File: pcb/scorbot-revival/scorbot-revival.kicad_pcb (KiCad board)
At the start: 2 copper layers, 30.5 x 76.2 mm, 4 parts, among them J1 DB-50, J2 Raspberry_Pi_2_3, U1 L293D, U2 PIC18F2431-E_SP

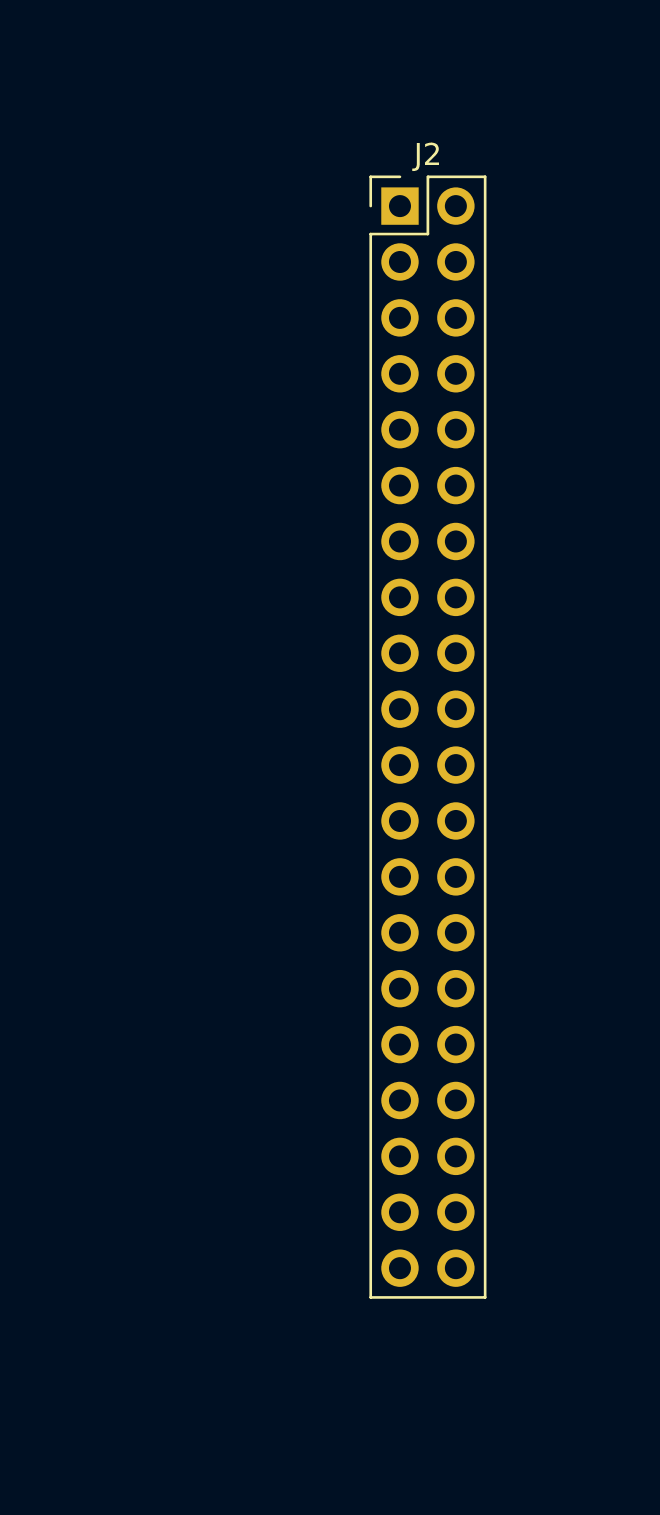
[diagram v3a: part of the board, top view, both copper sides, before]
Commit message: [pcb] update schematic connections
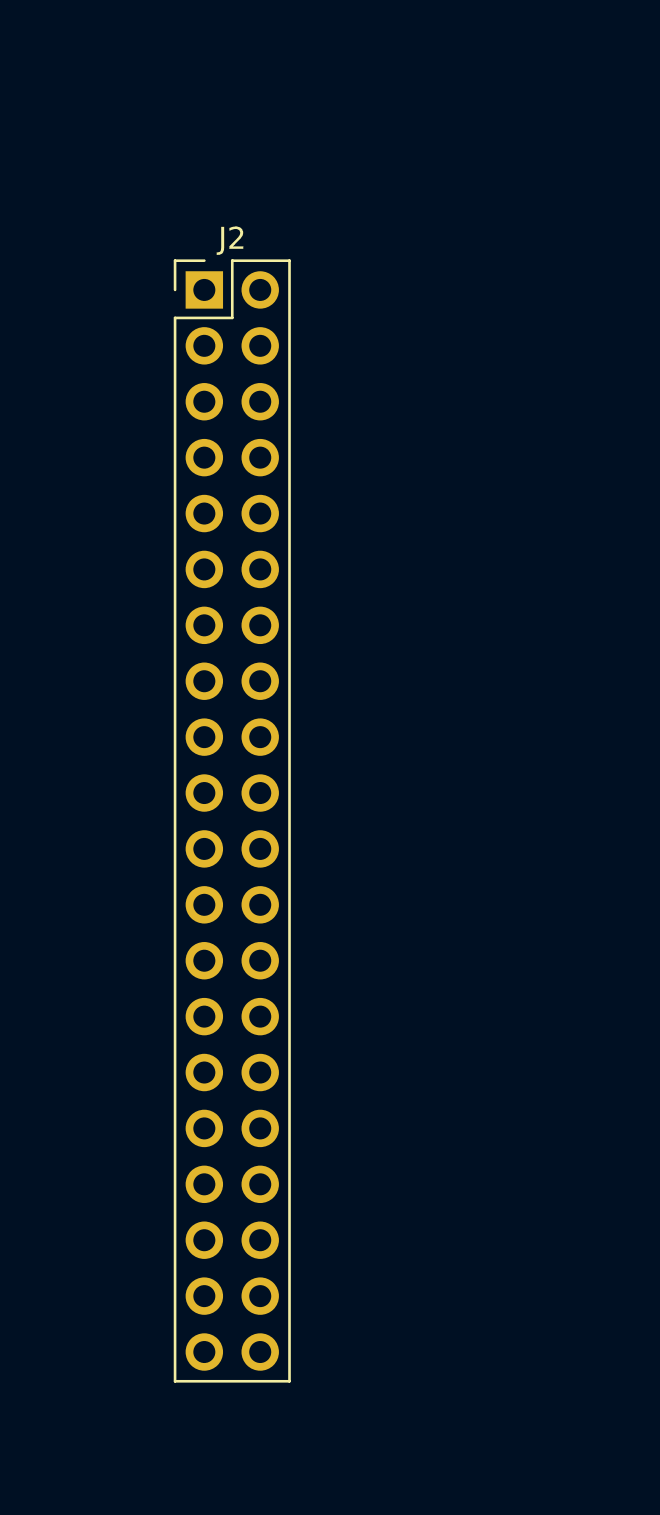
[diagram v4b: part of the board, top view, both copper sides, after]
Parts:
- moved J2 9.67 mm to (91.4, 30.5)
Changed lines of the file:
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@@
   )
   (module Connector_PinHeader_2.54mm:PinHeader_2x20_P2.54mm_Vertical (layer F.Cu)
-    (at 100.33 26.67)
+    (at 91.44 30.48)
     (descr "Through hole straight pin header, 2x20, 2.54mm pitch, double rows")
     (tags "Through hole pin header THT 2x20 2.54mm double row")

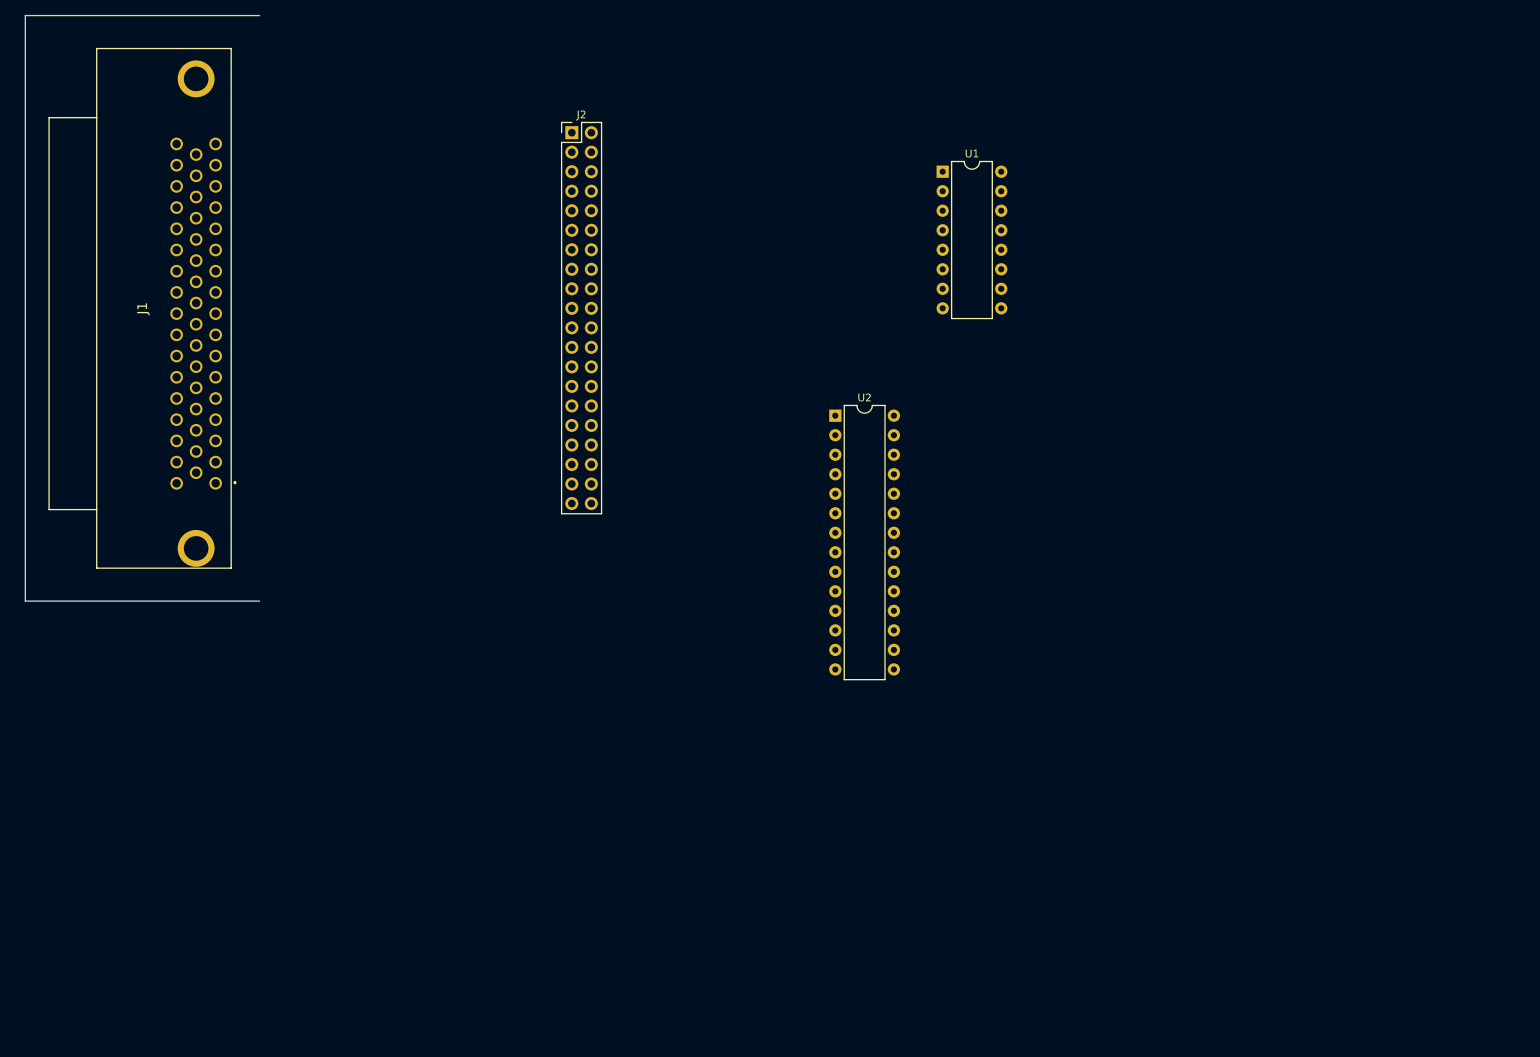
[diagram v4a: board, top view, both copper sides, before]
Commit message: [pcb] pcbnew updates
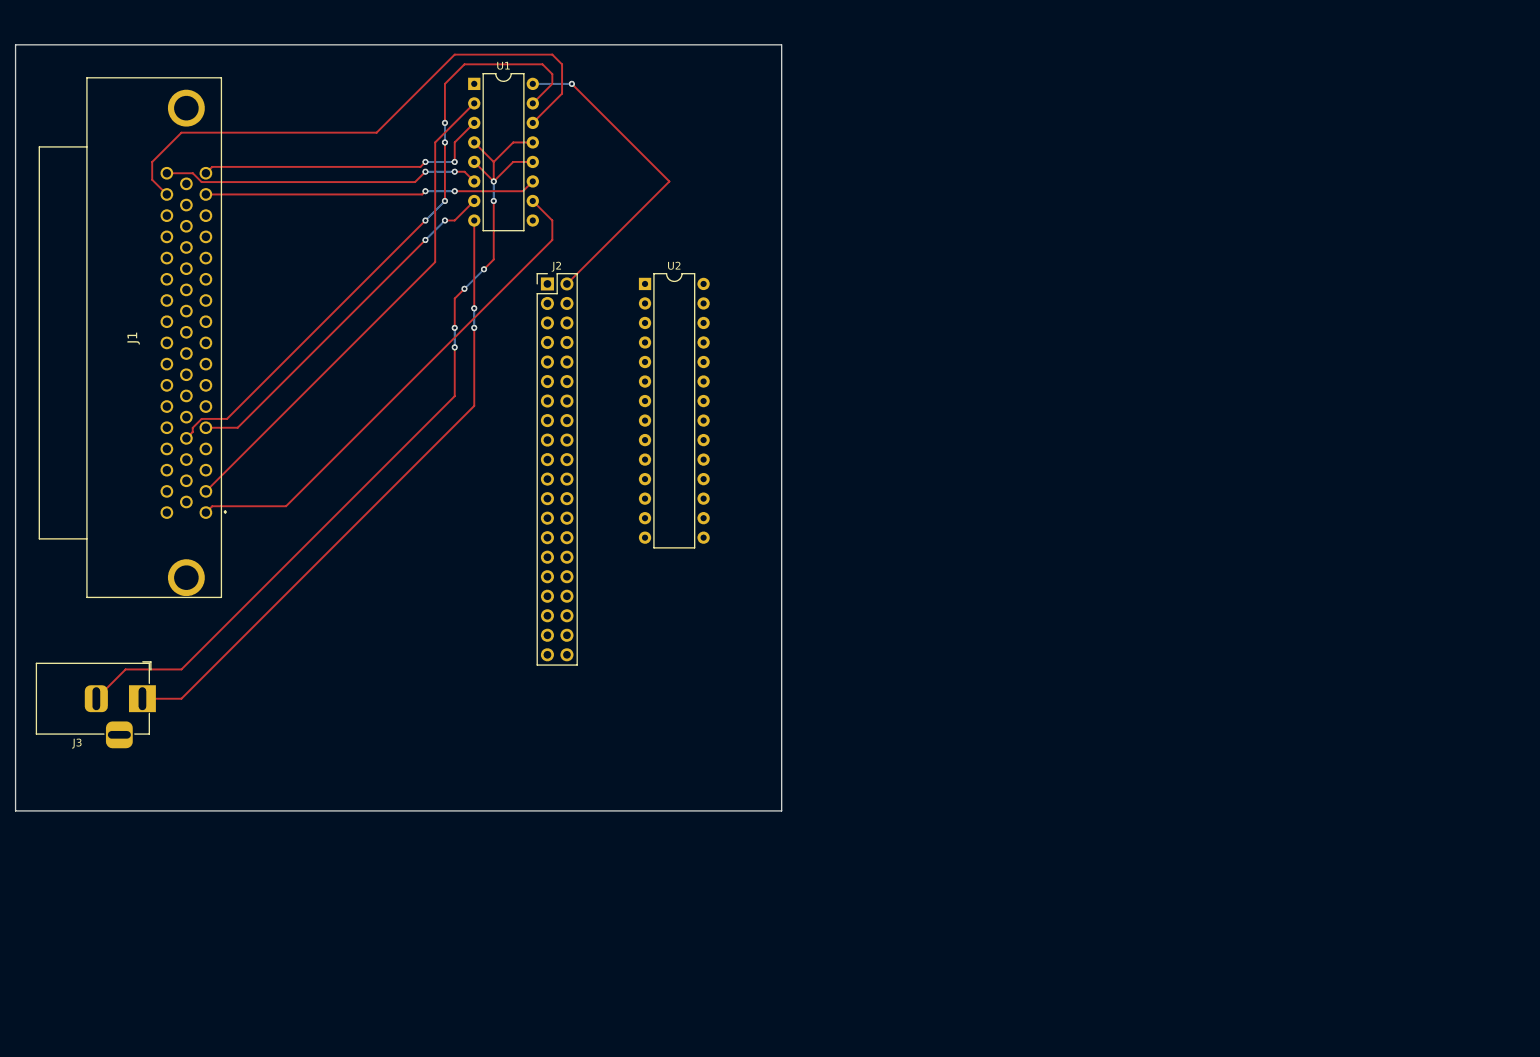
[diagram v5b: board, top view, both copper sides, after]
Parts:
- added J3: Conn_01x02, Connector_BarrelJack:BarrelJack_Horizontal, F.Cu at (35.6, 104.1)
- moved U1 62.0 mm to (78.7, 24.1)
- moved U2 30.1 mm to (101.0, 50.2)
- moved J2 19.9 mm to (88.3, 50.2)
- moved J1 4.02 mm to (34.3, 57.1)
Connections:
- J1 pad 1: (no net) -> /M2_LOGIC_P0
- J1 pad 10: (no net) -> /M3_LOGIC_LED
- J1 pad 11: (no net) -> /M1_LOGIC_LED
- J1 pad 12: (no net) -> /Grp+
- J1 pad 13: (no net) -> /M5+
- J1 pad 14: (no net) -> /M4+
- J1 pad 15: (no net) -> /M3+
- J1 pad 16: (no net) -> /M2+
- J1 pad 17: (no net) -> /M1+
- J1 pad 18: (no net) -> /M5_LOGIC_P0
- J1 pad 19: (no net) -> /Grp_LOGIC_P1
- J1 pad 2: (no net) -> /M1_LOGIC_P0
- J1 pad 20: (no net) -> /M4_LOGIC_P1
- J1 pad 21: (no net) -> /M2_LOGIC_P1
- J1 pad 22: (no net) -> /Grp_LOGIC_MS
- J1 pad 23: (no net) -> /M1_LOGIC_MS
- J1 pad 24: (no net) -> /M3_LOGIC_MS
- J1 pad 25: (no net) -> /Grp_LOGIC_LED
- J1 pad 26: (no net) -> /M4_LOGIC_LED
- J1 pad 27: (no net) -> /M2_LOGIC_LED
- J1 pad 3: (no net) -> /M5_LOGIC_P1
- J1 pad 34: (no net) -> /Grp_LOGIC_P0
- J1 pad 35: (no net) -> /M4_LOGIC_P0
- J1 pad 36: (no net) -> /M3_LOGIC_P0
- J1 pad 37: (no net) -> Net-(J1-Pad37)
- J1 pad 38: (no net) -> Net-(J1-Pad38)
- J1 pad 39: (no net) -> Net-(J1-Pad39)
- J1 pad 4: (no net) -> /M3_LOGIC_P1
- J1 pad 40: (no net) -> Net-(J1-Pad40)
- J1 pad 41: (no net) -> Net-(J1-Pad41)
- J1 pad 42: (no net) -> Net-(J1-Pad42)
- J1 pad 43: (no net) -> Net-(J1-Pad43)
- J1 pad 44: (no net) -> Net-(J1-Pad44)
- J1 pad 45: (no net) -> /Grp-
- J1 pad 46: (no net) -> /M5-
- J1 pad 47: (no net) -> /M4-
- J1 pad 48: (no net) -> /M3-
- J1 pad 49: (no net) -> /M2-
- J1 pad 5: (no net) -> /M1_LOGIC_P1
- J1 pad 50: (no net) -> /M1-
- J1 pad 6: (no net) -> /M5_LOGIC_MS
- J1 pad 7: (no net) -> /M2_LOGIC_MS
- J1 pad 8: (no net) -> /M4_LOGIC_MS
- J1 pad 9: (no net) -> /M5_LOGIC_LED
- J2 pad 1: (no net) -> Net-(J2-Pad1)
- J2 pad 10: (no net) -> Net-(J2-Pad10)
- J2 pad 11: (no net) -> Net-(J2-Pad11)
- J2 pad 12: (no net) -> Net-(J2-Pad12)
- J2 pad 13: (no net) -> Net-(J2-Pad13)
- J2 pad 15: (no net) -> /LOGIC_ENABLE_MOTORS
- J2 pad 16: (no net) -> Net-(J2-Pad16)
- J2 pad 17: (no net) -> Net-(J2-Pad17)
- J2 pad 18: (no net) -> Net-(J2-Pad18)
- J2 pad 19: (no net) -> Net-(J2-Pad19)
- J2 pad 2: (no net) -> /LOGIC_5V+
- J2 pad 21: (no net) -> Net-(J2-Pad21)
- J2 pad 22: (no net) -> Net-(J2-Pad22)
- J2 pad 23: (no net) -> Net-(J2-Pad23)
- J2 pad 24: (no net) -> Net-(J2-Pad24)
- J2 pad 26: (no net) -> Net-(J2-Pad26)
- J2 pad 27: (no net) -> Net-(J2-Pad27)
- J2 pad 28: (no net) -> Net-(J2-Pad28)
- J2 pad 29: (no net) -> Net-(J2-Pad29)
- J2 pad 3: (no net) -> Net-(J2-Pad3)
- J2 pad 31: (no net) -> Net-(J2-Pad31)
- J2 pad 32: (no net) -> Net-(J2-Pad32)
- J2 pad 33: (no net) -> Net-(J2-Pad33)
- J2 pad 34: (no net) -> /12V-
- J2 pad 35: (no net) -> Net-(J2-Pad35)
- J2 pad 36: (no net) -> Net-(J2-Pad36)
- J2 pad 37: (no net) -> Net-(J2-Pad37)
- J2 pad 38: (no net) -> Net-(J2-Pad38)
- J2 pad 39: (no net) -> Net-(J2-Pad39)
- J2 pad 4: (no net) -> Net-(J2-Pad4)
- J2 pad 40: (no net) -> Net-(J2-Pad40)
- J2 pad 5: (no net) -> Net-(J2-Pad5)
- J2 pad 7: (no net) -> Net-(J2-Pad7)
- J2 pad 8: (no net) -> Net-(J2-Pad8)
- U1 pad 1: (no net) -> /LOGIC_ENABLE_MOTORS
- U1 pad 10: (no net) -> /M2_LOGIC_P0
- U1 pad 11: (no net) -> /M2+
- U1 pad 12: (no net) -> /12V-
- U1 pad 13: (no net) -> /12V-
- U1 pad 14: (no net) -> /M2-
- U1 pad 15: (no net) -> /M2_LOGIC_P1
- U1 pad 16: (no net) -> /LOGIC_5V+
- U1 pad 2: (no net) -> /M1_LOGIC_P0
- U1 pad 3: (no net) -> /M1+
- U1 pad 4: (no net) -> /12V-
- U1 pad 5: (no net) -> /12V-
- U1 pad 6: (no net) -> /M1-
- U1 pad 7: (no net) -> /M1_LOGIC_P1
- U1 pad 8: (no net) -> /12V+
- U1 pad 9: (no net) -> /LOGIC_ENABLE_MOTORS
- U2 pad 1: (no net) -> Net-(U2-Pad1)
- U2 pad 10: (no net) -> Net-(U2-Pad10)
- U2 pad 11: (no net) -> Net-(U2-Pad11)
- U2 pad 12: (no net) -> Net-(U2-Pad12)
- U2 pad 13: (no net) -> Net-(U2-Pad13)
- U2 pad 14: (no net) -> Net-(U2-Pad14)
- U2 pad 15: (no net) -> Net-(U2-Pad15)
- U2 pad 16: (no net) -> Net-(U2-Pad16)
- U2 pad 17: (no net) -> Net-(U2-Pad17)
- U2 pad 18: (no net) -> Net-(U2-Pad18)
- U2 pad 19: (no net) -> Net-(U2-Pad19)
- U2 pad 2: (no net) -> Net-(U2-Pad2)
- U2 pad 20: (no net) -> Net-(U2-Pad20)
- U2 pad 21: (no net) -> Net-(U2-Pad21)
- U2 pad 22: (no net) -> Net-(U2-Pad22)
- U2 pad 23: (no net) -> Net-(U2-Pad23)
- U2 pad 24: (no net) -> Net-(U2-Pad24)
- U2 pad 25: (no net) -> Net-(U2-Pad25)
- U2 pad 26: (no net) -> Net-(U2-Pad26)
- U2 pad 27: (no net) -> Net-(U2-Pad27)
- U2 pad 28: (no net) -> Net-(U2-Pad28)
- U2 pad 3: (no net) -> Net-(U2-Pad3)
- U2 pad 4: (no net) -> Net-(U2-Pad4)
- U2 pad 5: (no net) -> Net-(U2-Pad5)
- U2 pad 6: (no net) -> Net-(U2-Pad6)
- U2 pad 7: (no net) -> Net-(U2-Pad7)
- U2 pad 8: (no net) -> Net-(U2-Pad8)
- U2 pad 9: (no net) -> Net-(U2-Pad9)
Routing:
- net /12V-: track 0.00 -> 115.0 mm, vias 0 -> 6
- net /12V+: track 0.00 -> 83.1 mm, vias 0 -> 2
- net /M2_LOGIC_P1: track 0.00 -> 82.4 mm, vias 0 -> 4
- net /M2-: track 0.00 -> 73.9 mm
- net /M2_LOGIC_P0: track 0.00 -> 65.9 mm
- net /M1_LOGIC_P0: track 0.00 -> 65.0 mm
- net /M1_LOGIC_P1: track 0.00 -> 47.1 mm, vias 0 -> 2
- net /M2+: track 0.00 -> 43.2 mm, vias 0 -> 2
- net /LOGIC_5V+: track 0.00 -> 41.9 mm, vias 0 -> 1
- net /M1-: track 0.00 -> 41.6 mm, vias 0 -> 2
- net /M1+: track 0.00 -> 39.1 mm, vias 0 -> 2
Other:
- board size 30.5 x 76.2 mm -> 99.7 x 99.7 mm

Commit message: finished trace conections
added trace and simplifyed
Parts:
- turned J3 to 90 degrees
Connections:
- J1 pad 17: /M1+ -> /M2-
- J1 pad 51: (no net) -> /M2-
- U1 pad 3: /M1+ -> /M2-
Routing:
- net /Grp_LOGIC_GND: track 0.00 -> 72.0 mm
- net /M5_LOGIC_GND: track 0.00 -> 63.7 mm
- net /M4_LOGIC_GND: track 0.00 -> 61.0 mm
- net /M3_LOGIC_GND: track 0.00 -> 58.9 mm
- net /M1_LOGIC_GND: track 0.00 -> 57.0 mm
- net /M2_LOGIC_GND: track 0.00 -> 55.4 mm
- net /M2-: track 73.9 -> 123.0 mm
- net /12V-: track 115.0 -> 161.2 mm, vias 6 -> 7
- net /M1+: track 39.1 -> 0.00 mm, vias 2 -> 0
- net /LOGIC_ENABLE_MOTORS: track 0.00 -> 28.9 mm, vias 0 -> 1
- net /M1_LOGIC_P0: track 65.0 -> 65.6 mm, vias 0 -> 1
- net /M1_LOGIC_P1: vias 2 -> 1
- net /M2_LOGIC_P1: vias 4 -> 2
- net /M2+: vias 2 -> 0
- net /M1-: vias 2 -> 0

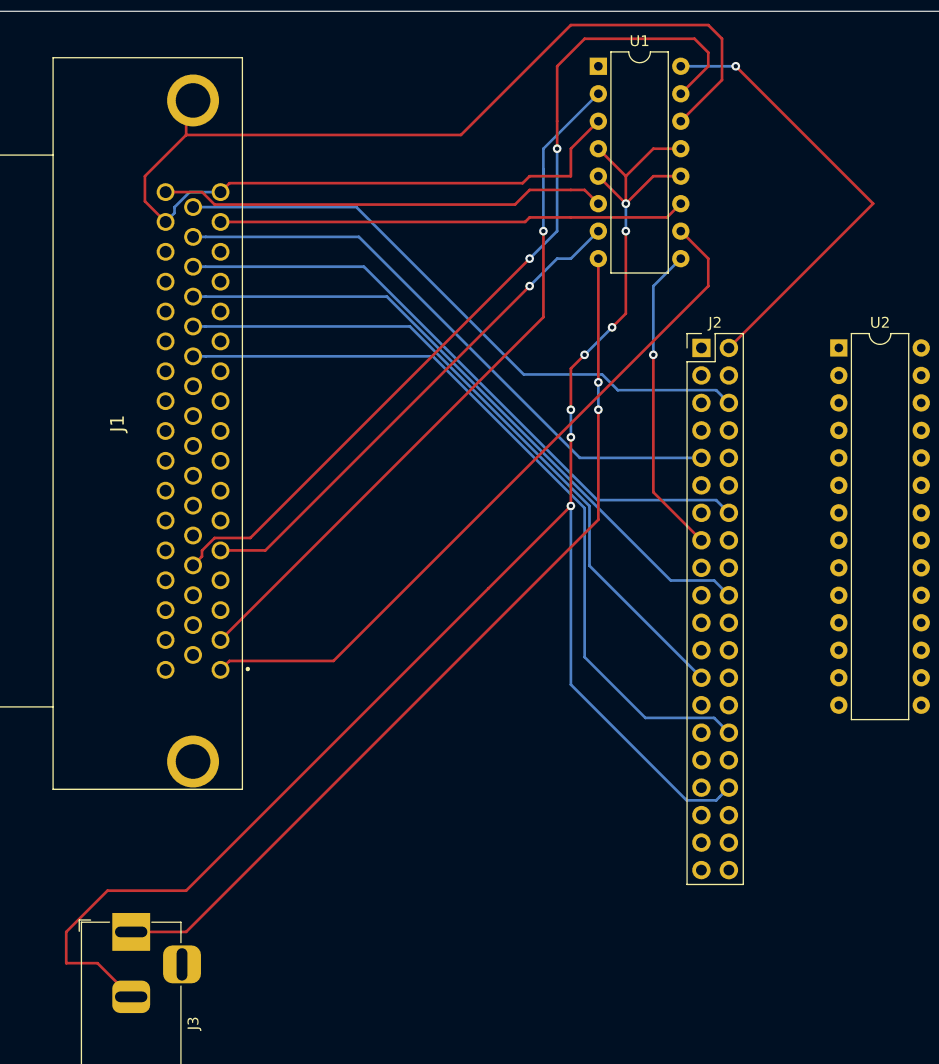
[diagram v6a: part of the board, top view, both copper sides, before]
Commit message: Added more L293Ds to net
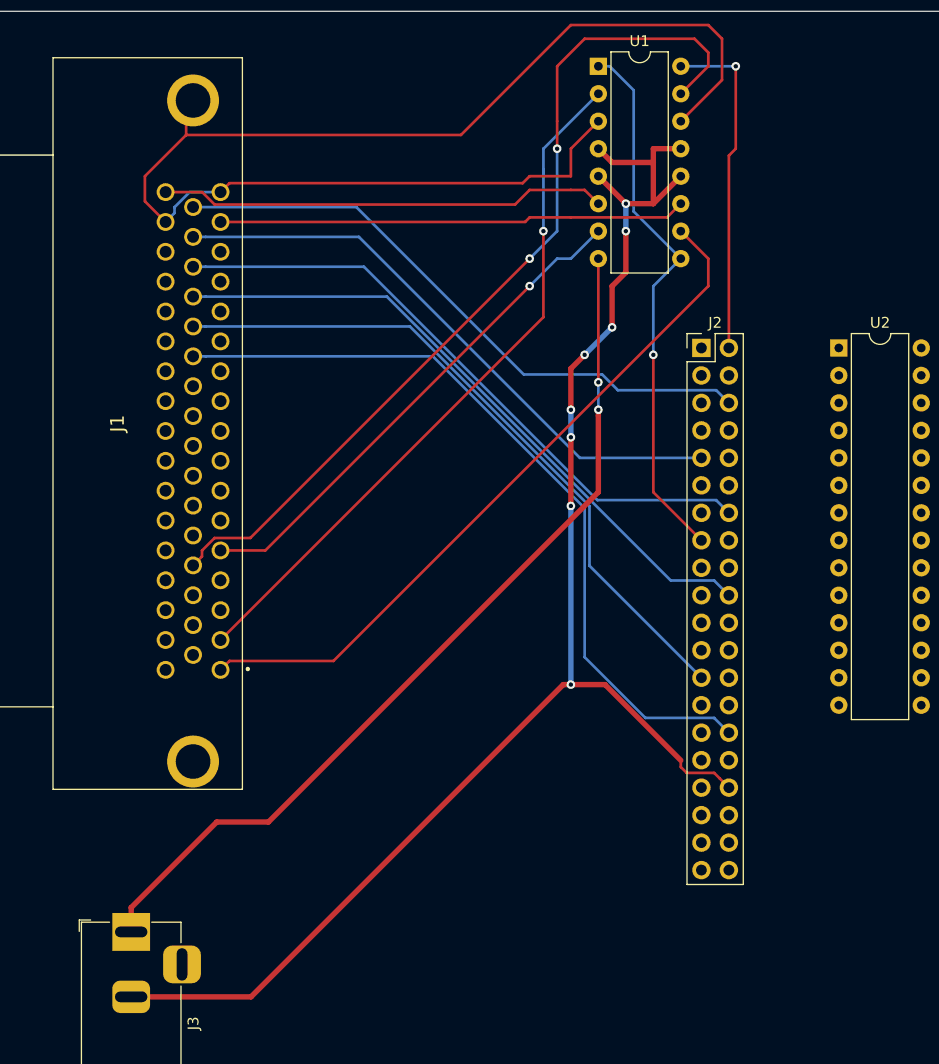
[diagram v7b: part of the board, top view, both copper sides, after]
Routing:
- net /LOGIC_ENABLE_MOTORS: track 28.9 -> 50.5 mm
- net /12V-: track 161.2 -> 141.0 mm, vias 7 -> 8
- net /LOGIC_5V+: track 41.9 -> 31.4 mm
